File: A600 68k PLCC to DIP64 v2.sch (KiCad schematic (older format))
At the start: 6 parts, among them U1 MC68000_PLCC68, U2 68000_SOCKET

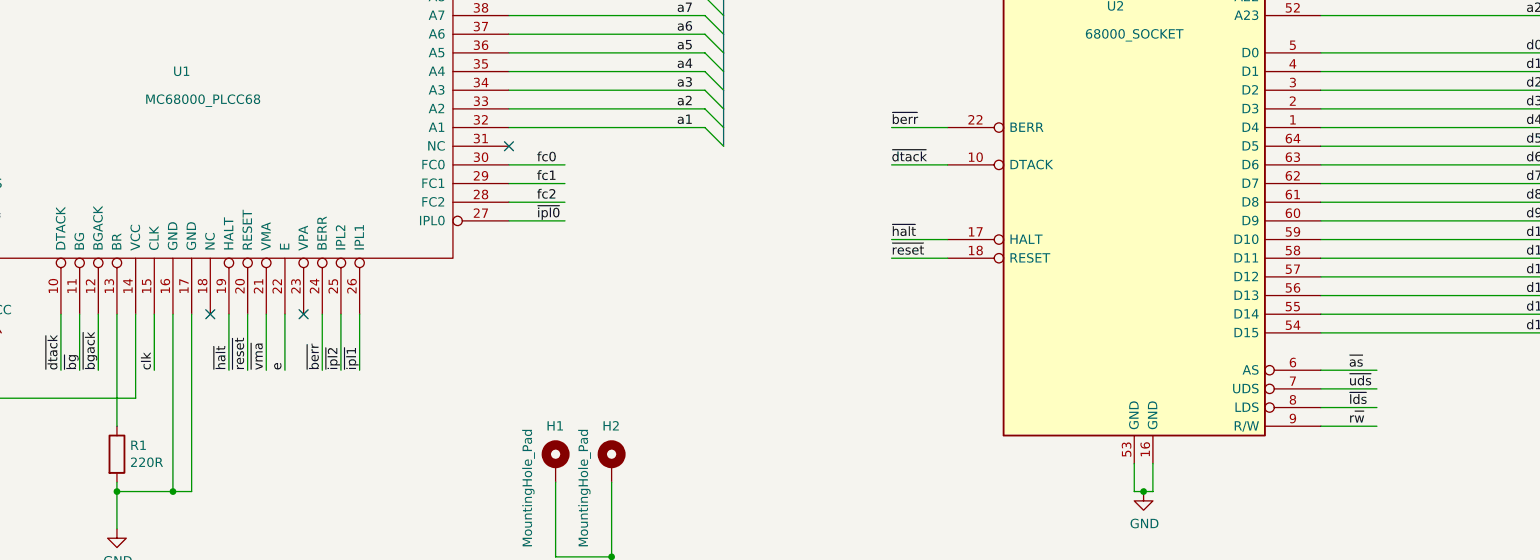
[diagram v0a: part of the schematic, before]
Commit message: updated VCC handling
updated PLCC nets to have extra VCC lines from N/C pins to better support thirsty cards like PiStorm.
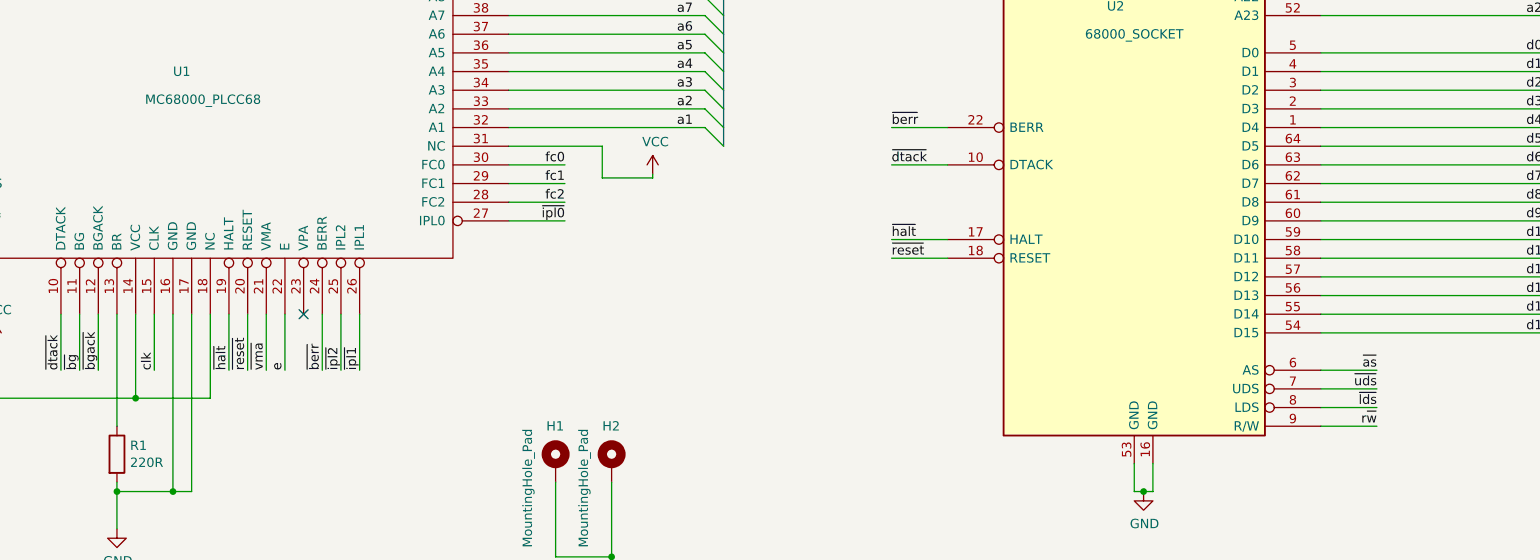
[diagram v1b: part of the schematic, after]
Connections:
- wire segments 188 -> 194
- no-connect marks 3 -> 1
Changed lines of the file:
@@
 	3050 6150 2950 6150
 Connection ~ 2950 6150
-NoConn ~ 3150 5200
 NoConn ~ 3650 5200
 $Comp
@@
 	8200 950  8150 950
 Connection ~ 8150 950
-NoConn ~ 4750 4300
 Wire Wire Line
 	1550 4300 1000 4300
@@
 Text Label 3950 5500 1    50   ~ 0
 ~ipl1
-Text Label 4900 4400 0    50   ~ 0
+Text Label 5050 4400 2    50   ~ 0
 fc0
-Text Label 4900 4500 0    50   ~ 0
+Text Label 5050 4500 2    50   ~ 0
 fc1
-Text Label 4900 4600 0    50   ~ 0
+Text Label 5050 4600 2    50   ~ 0
 fc2
-Text Label 4900 4700 0    50   ~ 0
+Text Label 5050 4700 2    50   ~ 0
 ~ipl0
 Text Label 6800 1400 0    50   ~ 0
@@
 Text Label 6800 4900 0    50   ~ 0
 ~reset
-Text Label 9250 5500 0    50   ~ 0
+Text Label 9400 5500 2    50   ~ 0
 ~as
-Text Label 9250 5600 0    50   ~ 0
+Text Label 9400 5600 2    50   ~ 0
 ~uds
-Text Label 9250 5700 0    50   ~ 0
+Text Label 9400 5700 2    50   ~ 0
 ~lds
-Text Label 9250 5800 0    50   ~ 0
+Text Label 9400 5800 2    50   ~ 0
 r~w
 $Comp
@@
 Wire Wire Line
 	5300 6500 5300 6600
+Wire Wire Line
+	3150 5200 3150 5650
+Wire Wire Line
+	3150 5650 2750 5650
+Connection ~ 2750 5650
+Wire Wire Line
+	4750 4300 5250 4300
+Wire Wire Line
+	5250 4300 5250 4470
+Wire Wire Line
+	5250 4470 5520 4470
+Wire Wire Line
+	5520 4470 5520 4450
+$Comp
+L power:VCC #PWR?
+U 1 1 60F27F01
+P 5520 4450
+F 0 "#PWR?" H 5520 4300 50  0001 C CNN
+F 1 "VCC" H 5535 4623 50  0000 C CNN
+F 2 "" H 5520 4450 50  0001 C CNN
+F 3 "" H 5520 4450 50  0001 C CNN
+	1    5520 4450
+	1    0    0    -1
+$EndComp
 Wire Bus Line
 	10450 3900 10450 5400
